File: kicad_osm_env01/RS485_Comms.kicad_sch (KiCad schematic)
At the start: 17 parts, among them U7 ST3485EBDR

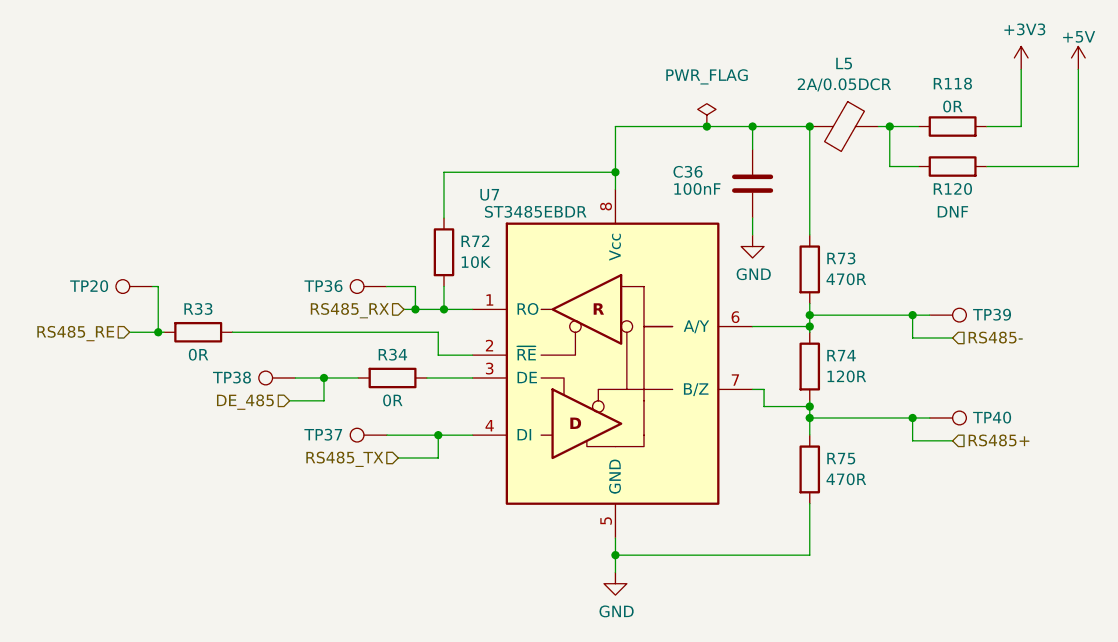
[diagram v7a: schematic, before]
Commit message: removed 0R links and DNF parts on schematics
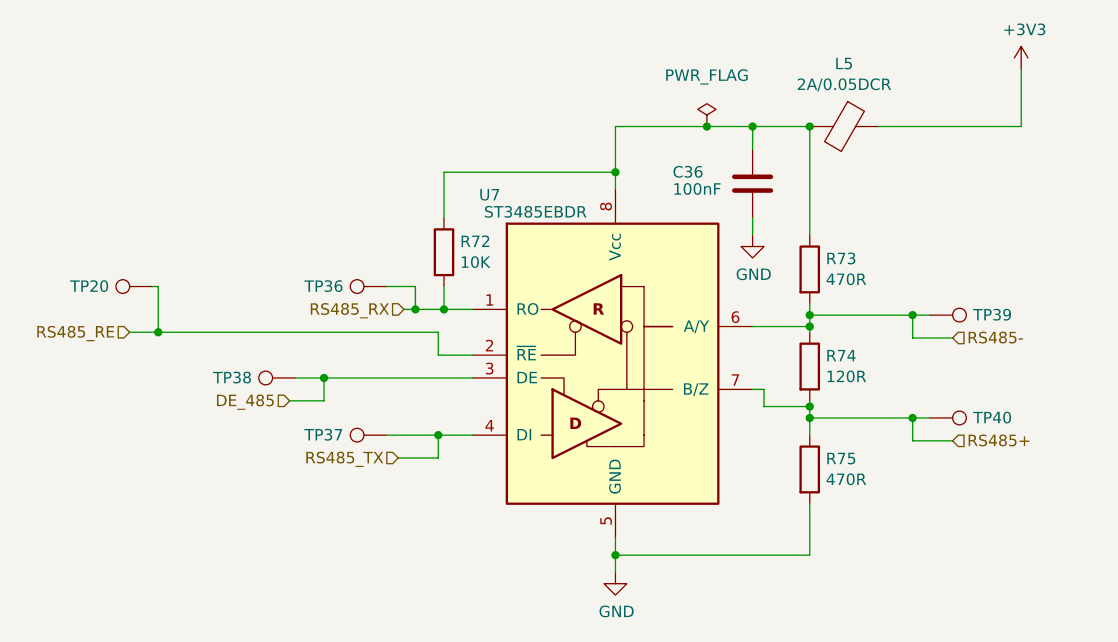
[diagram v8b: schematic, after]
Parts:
- removed R118, R33, R34: 0R, Resistor_SMD:R_0402_1005Metric, symbol Device:R
- removed R120: DNF, Resistor_SMD:R_0402_1005Metric, symbol Device:R
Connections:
- net +3V3: now also L5.1
- net DE_485: now also U7.3 (DE)
- net RS485_RE: now also U7.2 (~{RE})
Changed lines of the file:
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@@
     (comment 1 "Part No: 304-010")
   )
-  (junction (at 173.99 71.755) (diameter 0) (color 0 0 0 0)
-  )
   (junction (at 176.53 104.14) (diameter 0) (color 0 0 0 0)
   )
@@
   (junction (at 124.46 92.075) (diameter 0) (color 0 0 0 0)
   )
-  (wire (pts (xy 172.72 71.755) (xy 173.99 71.755))
-    (stroke (width 0) (type default))
-  )
   (wire (pts (xy 158.75 83.82) (xy 158.75 81.915))
     (stroke (width 0) (type default))
@@
     (stroke (width 0) (type default))
   )
-  (wire (pts (xy 184.785 76.2) (xy 194.945 76.2))
-    (stroke (width 0) (type default))
-  )
   (wire (pts (xy 165.1 104.14) (xy 176.53 104.14))
     (stroke (width 0) (type default))
@@
     (stroke (width 0) (type default))
   )
-  (wire (pts (xy 184.785 71.755) (xy 188.595 71.755))
+  (wire (pts (xy 172.72 71.755) (xy 188.595 71.755))
     (stroke (width 0) (type default))
   )
@@
     (stroke (width 0) (type default))
   )
-  (wire (pts (xy 100.965 94.615) (xy 123.825 94.615))
-    (stroke (width 0) (type default))
-  )
   (wire (pts (xy 124.46 81.915) (xy 124.46 76.835))
     (stroke (width 0) (type default))
@@
     (stroke (width 0) (type default))
   )
-  (wire (pts (xy 173.99 71.755) (xy 177.165 71.755))
-    (stroke (width 0) (type default))
-  )
-  (wire (pts (xy 194.945 65.405) (xy 194.945 76.2))
-    (stroke (width 0) (type default))
-  )
   (wire (pts (xy 121.285 89.535) (xy 121.285 92.075))
     (stroke (width 0) (type default))
   )
-  (wire (pts (xy 111.125 99.695) (xy 114.935 99.695))
+  (wire (pts (xy 111.125 99.695) (xy 127.635 99.695))
     (stroke (width 0) (type default))
   )
@@
     (stroke (width 0) (type default))
   )
-  (wire (pts (xy 177.165 76.2) (xy 173.99 76.2))
-    (stroke (width 0) (type default))
-  )
   (wire (pts (xy 123.825 106.045) (xy 127.635 106.045))
     (stroke (width 0) (type default))
@@
     (stroke (width 0) (type default))
   )
-  (wire (pts (xy 127.635 99.695) (xy 122.555 99.695))
-    (stroke (width 0) (type default))
-  )
   (wire (pts (xy 123.825 108.585) (xy 123.825 106.045))
     (stroke (width 0) (type default))
@@
     (stroke (width 0) (type default))
   )
-  (wire (pts (xy 173.99 76.2) (xy 173.99 71.755))
-    (stroke (width 0) (type default))
-  )
   (wire (pts (xy 165.1 93.98) (xy 158.75 93.98))
     (stroke (width 0) (type default))
@@
     (stroke (width 0) (type default))
   )
-  (wire (pts (xy 93.345 94.615) (xy 92.71 94.615))
+  (wire (pts (xy 92.71 94.615) (xy 123.825 94.615))
     (stroke (width 0) (type default))
   )
@@
     )
   )
-  (symbol (lib_id "Device:R") (at 118.745 99.695 270) (unit 1)
-    (in_bom yes) (on_board yes) (dnp no)
-    (property "Reference" "R34" (at 118.745 97.155 90)
-      (effects (font (size 1.27 1.27)))
-    )
-    (property "Value" "0R" (at 118.745 102.235 90)
-      (effects (font (size 1.27 1.27)))
-    )
-    (property "Footprint" "Resistor_SMD:R_0402_1005Metric" (at 118.745 97.917 90)
-      (effects (font (size 1.27 1.27)) hide)
-    )
-    (property "Datasheet" "" (at 118.745 99.695 0)
-      (effects (font (size 1.27 1.27)) hide)
-    )
-    (property "Tolerance" "1%" (at 118.745 99.695 0)
-      (effects (font (size 1.27 1.27)) hide)
-    )
-    (property "Power Rating" "" (at 118.745 99.695 0)
-      (effects (font (size 1.27 1.27)) hide)
-    )
-    (property "Current Rating" "" (at 118.745 99.695 0)
-      (effects (font (size 1.27 1.27)) hide)
-    )
-    (pin "1")
-    (pin "2")
-    (instances
-      (project "OSM_env01"
-        (path "/ab8b0540-9c9f-4195-88f5-7bed0b0a8ed6/00000000-0000-0000-0000-0000609d4b87"
-          (reference "R34") (unit 1)
-        )
-      )
-    )
-  )
-  (symbol (lib_id "Device:R") (at 97.155 94.615 270) (unit 1)
-    (in_bom yes) (on_board yes) (dnp no)
-    (property "Reference" "R33" (at 97.155 92.075 90)
-      (effects (font (size 1.27 1.27)))
-    )
-    (property "Value" "0R" (at 97.155 97.155 90)
-      (effects (font (size 1.27 1.27)))
-    )
-    (property "Footprint" "Resistor_SMD:R_0402_1005Metric" (at 97.155 92.837 90)
-      (effects (font (size 1.27 1.27)) hide)
-    )
-    (property "Datasheet" "" (at 97.155 94.615 0)
-      (effects (font (size 1.27 1.27)) hide)
-    )
-    (property "Tolerance" "1%" (at 97.155 94.615 0)
-      (effects (font (size 1.27 1.27)) hide)
-    )
-    (property "Power Rating" "" (at 97.155 94.615 0)
-      (effects (font (size 1.27 1.27)) hide)
-    )
-    (property "Current Rating" "" (at 97.155 94.615 0)
-      (effects (font (size 1.27 1.27)) hide)
-    )
-    (pin "1")
-    (pin "2")
-    (instances
-      (project "OSM_env01"
-        (path "/ab8b0540-9c9f-4195-88f5-7bed0b0a8ed6/00000000-0000-0000-0000-0000609d4b87"
-          (reference "R33") (unit 1)
-        )
-      )
-    )
-  )
   (symbol (lib_id "power:+3V3") (at 188.595 65.405 0) (unit 1)
     (in_bom yes) (on_board yes) (dnp no)
@@
         )
       )
-    )
-  )
-  (symbol (lib_id "Device:R") (at 180.975 76.2 90) (unit 1)
-    (in_bom yes) (on_board yes) (dnp no)
-    (property "Reference" "R120" (at 180.975 78.74 90)
-      (effects (font (size 1.27 1.27)))
-    )
-    (property "Value" "DNF" (at 180.975 81.28 90)
-      (effects (font (size 1.27 1.27)))
-    )
-    (property "Footprint" "Resistor_SMD:R_0402_1005Metric" (at 180.975 77.978 90)
-      (effects (font (size 1.27 1.27)) hide)
-    )
-    (property "Datasheet" "" (at 180.975 76.2 0)
-      (effects (font (size 1.27 1.27)) hide)
-    )
-    (property "Tolerance" "1%" (at 180.975 76.2 0)
-      (effects (font (size 1.27 1.27)) hide)
-    )
-    (property "Power Rating" "" (at 180.975 76.2 0)
-      (effects (font (size 1.27 1.27)) hide)
-    )
-    (property "Current Rating" "" (at 180.975 76.2 0)
-      (effects (font (size 1.27 1.27)) hide)
-    )
-    (pin "1")
-    (pin "2")
-    (instances
-      (project "OSM_env01"
-        (path "/ab8b0540-9c9f-4195-88f5-7bed0b0a8ed6/00000000-0000-0000-0000-0000609d4b87"
-          (reference "R120") (unit 1)
-        )
-      )
-    )
-  )
-  (symbol (lib_id "Device:R") (at 180.975 71.755 90) (unit 1)
-    (in_bom yes) (on_board yes) (dnp no) (fields_autoplaced)
-    (property "Reference" "R118" (at 180.975 67.0392 90)
-      (effects (font (size 1.27 1.27)))
-    )
-    (property "Value" "0R" (at 180.975 69.5761 90)
-      (effects (font (size 1.27 1.27)))
-    )
-    (property "Footprint" "Resistor_SMD:R_0402_1005Metric" (at 180.975 73.533 90)
-      (effects (font (size 1.27 1.27)) hide)
-    )
-    (property "Datasheet" "" (at 180.975 71.755 0)
-      (effects (font (size 1.27 1.27)) hide)
-    )
-    (property "Tolerance" "1%" (at 180.975 71.755 0)
-      (effects (font (size 1.27 1.27)) hide)
-    )
-    (property "Power Rating" "" (at 180.975 71.755 0)
-      (effects (font (size 1.27 1.27)) hide)
-    )
-    (property "Current Rating" "" (at 180.975 71.755 0)
-      (effects (font (size 1.27 1.27)) hide)
-    )
-    (pin "1")
-    (pin "2")
-    (instances
-      (project "OSM_env01"
-        (path "/ab8b0540-9c9f-4195-88f5-7bed0b0a8ed6/00000000-0000-0000-0000-0000609d4b87"
-          (reference "R118") (unit 1)
-        )
-      )
-    )
-  )
-  (symbol (lib_id "OSM_env01:+5V") (at 194.945 65.405 0) (unit 1)
-    (in_bom yes) (on_board yes) (dnp no) (fields_autoplaced)
-    (property "Reference" "#PWR096" (at 194.945 69.215 0)
-      (effects (font (size 1.27 1.27)) hide)
-    )
-    (property "Value" "+5V" (at 194.945 61.8292 0)
-      (effects (font (size 1.27 1.27)))
-    )
-    (property "Footprint" "" (at 194.945 65.405 0)
-      (effects (font (size 1.524 1.524)))
-    )
-    (property "Datasheet" "" (at 194.945 65.405 0)
-      (effects (font (size 1.524 1.524)))
-    )
-    (pin "1")
-    (instances
-      (project "OSM_env01"
-        (path "/ab8b0540-9c9f-4195-88f5-7bed0b0a8ed6/00000000-0000-0000-0000-0000609d4b87"
-          (reference "#PWR096") (unit 1)
-        )
-      )
